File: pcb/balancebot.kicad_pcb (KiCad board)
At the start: 2 copper layers, 31 parts, among them J1 Conn_01x04, J2 Conn_01x02, J3 Conn_01x03, J4 Conn_01x04, J5 Conn_01x04, J6 Conn_01x07, U1 LSM6DS3, U2 DRV8835, U3 ESP32mini, U4 DSN-MINI-360

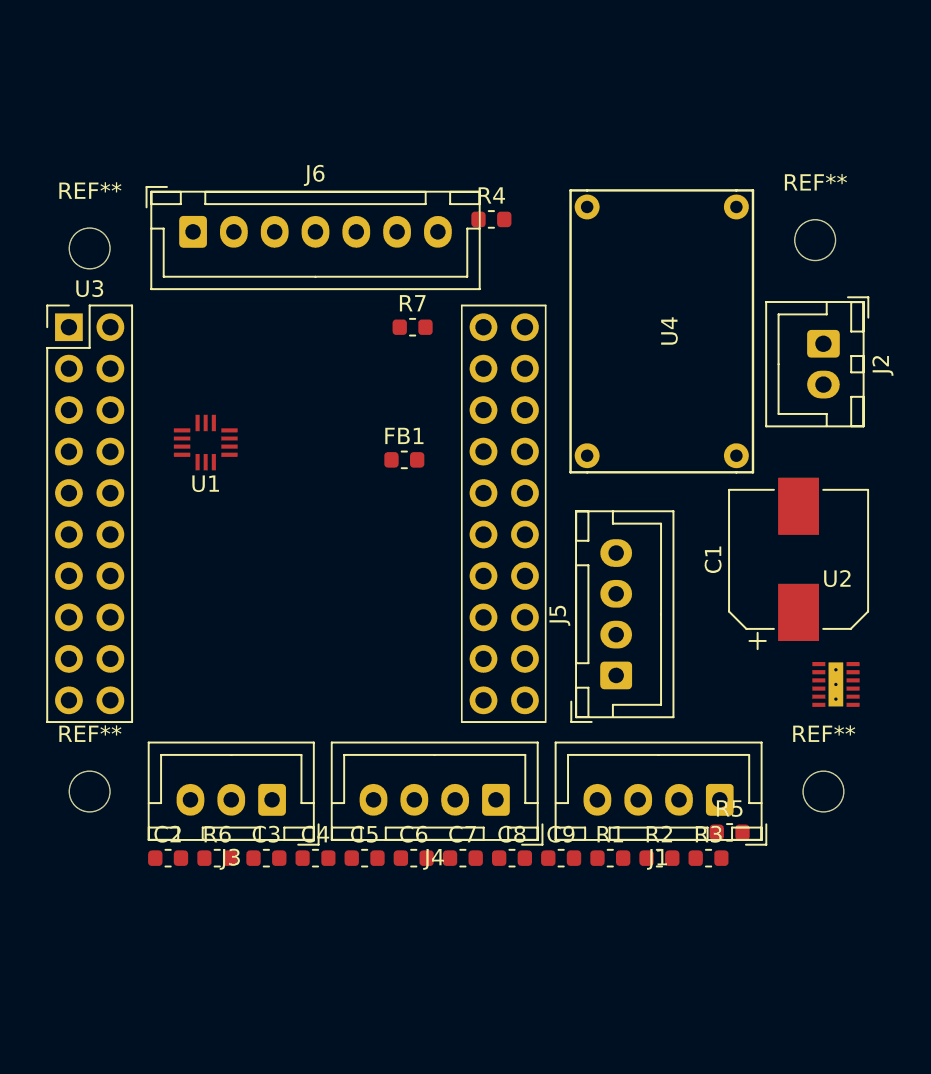
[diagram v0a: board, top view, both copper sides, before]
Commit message: Fix ESP32 footprint.
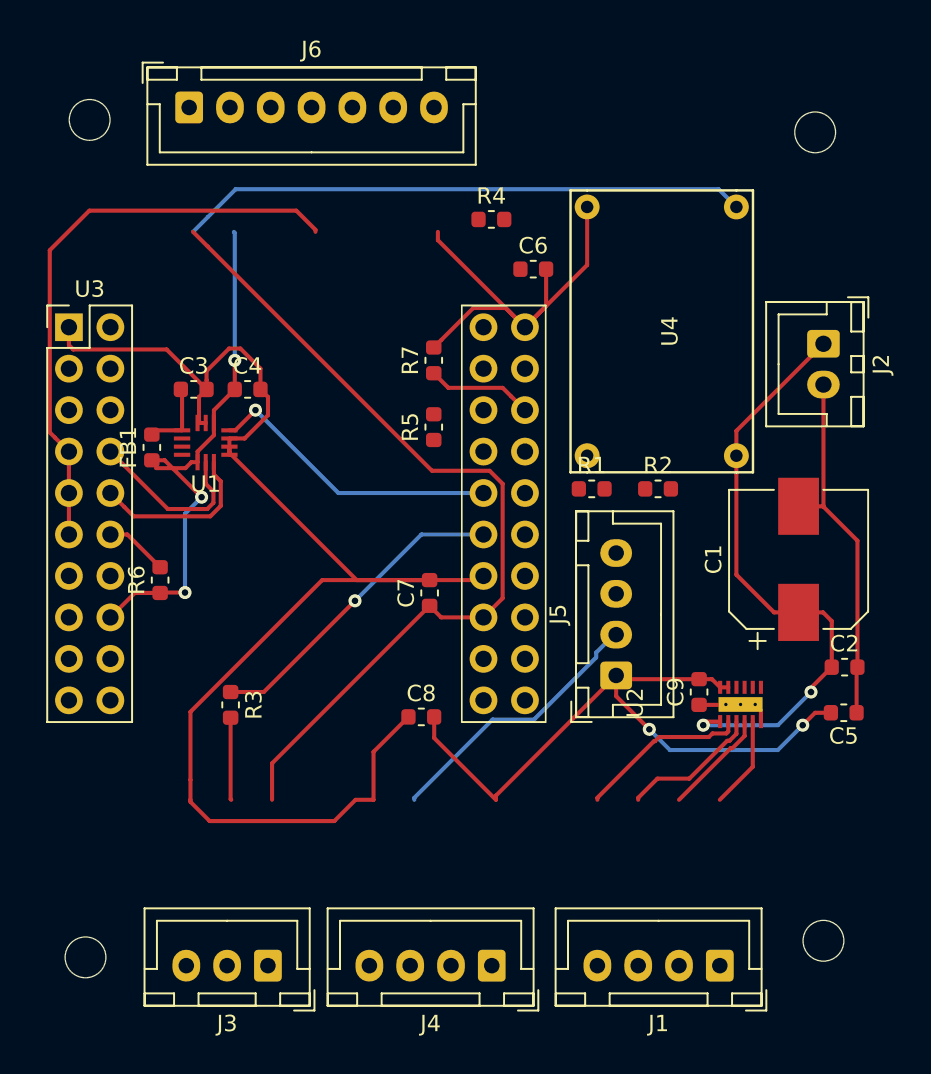
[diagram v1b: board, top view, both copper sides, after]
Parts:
- moved C2 43.1 mm to (164.9, 88.6)
- moved C6 36.8 mm to (145.8, 64.3)
- moved R3 30.8 mm to (127.3, 91.0), turned to 270 degrees
- moved R5 30.7 mm to (139.7, 73.9), turned to 90 degrees
- moved C5 30.7 mm to (164.8, 91.4), turned to 180 degrees
- moved C3 29.1 mm to (125.0, 71.6)
- moved C4 29.0 mm to (128.3, 71.6)
- moved R1 22.7 mm to (149.4, 77.7)
- moved R2 22.6 mm to (153.4, 77.7)
- moved R6 17.4 mm to (122.9, 83.3), turned to 90 degrees
- moved C7 16.4 mm to (139.4, 84.1), turned to 90 degrees
- moved FB1 15.5 mm to (122.4, 75.2), turned to 90 degrees
- moved C9 13.2 mm to (156.0, 90.2), turned to 90 degrees
- moved C8 10.3 mm to (138.9, 91.7)
- moved J3 10.2 mm to (129.5, 106.9)
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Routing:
- net GND: track 0.00 -> 140.3 mm
- net +5V: track 0.00 -> 88.3 mm
- net +3V3: track 0.00 -> 74.5 mm, vias 0 -> 5
- net Net-(J4-Pad3): track 0.00 -> 52.6 mm
- net +BATT: track 0.00 -> 36.8 mm, vias 0 -> 2
- net Net-(R3-Pad1): track 0.00 -> 19.5 mm, vias 0 -> 1
- net IO17: track 0.00 -> 18.2 mm, vias 0 -> 1
- net IO18: track 0.00 -> 10.6 mm
- net IO19: track 0.00 -> 10.5 mm
- net Net-(J1-Pad4): track 0.00 -> 10.4 mm
- net Net-(J1-Pad3): track 0.00 -> 8.52 mm
- net BENBL: track 0.00 -> 6.52 mm
- net Net-(J1-Pad2): track 0.00 -> 6.52 mm
- net Net-(J1-Pad1): track 0.00 -> 5.63 mm
- net Net-(J3-Pad2): track 0.00 -> 5.05 mm
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
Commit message: Complete routing.
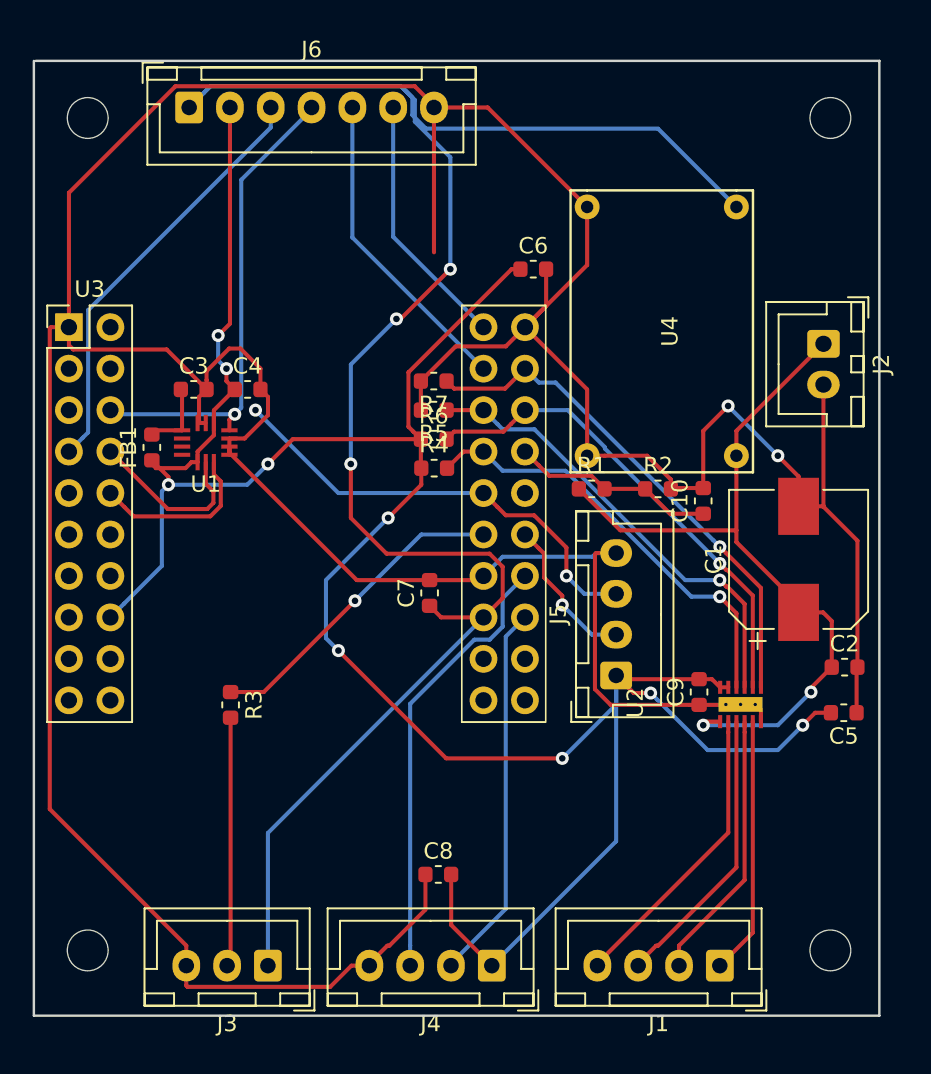
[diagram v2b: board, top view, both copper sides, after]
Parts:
- removed the REF** at (118.4, 106.4)
- removed the REF** at (118.6, 55.1)
- removed the REF** at (163.1, 55.9)
- removed the REF** at (163.6, 105.4)
- added C10: 100n, Capacitor_SMD:C_0603_1608Metric, F.Cu at (156.2, 78.5)
- added REF**: MountingHole_2.5mm, MountingHole:MountingHole_2.5mm, F.Cu at (118.5, 106.0)
- added REF**: MountingHole_2.5mm, MountingHole:MountingHole_2.5mm, F.Cu at (164.0, 106.0)
- added REF**: MountingHole_2.5mm, MountingHole:MountingHole_2.5mm, F.Cu at (164.0, 55.0)
- added REF**: MountingHole_2.5mm, MountingHole:MountingHole_2.5mm, F.Cu at (118.5, 55.0)
- U3: footprint modules:ESP32mini -> BalanceBot:ESP32mini
- U4: footprint dsn-mini-360:DSN-MINI-360 -> BalanceBot:DSN-MINI-360
- moved R6 18.9 mm to (139.7, 74.7), turned to 0 degrees
- moved R4 15.6 mm to (139.7, 76.5)
- moved C8 9.71 mm to (140.0, 101.3)
- moved R7 1.27 mm to (139.7, 71.1), turned to 180 degrees
- moved R5 1.04 mm to (139.7, 72.9), turned to 180 degrees
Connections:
- J4 pad 2: Net-(J4-Pad2) -> IO2
- J4 pad 3: Net-(J4-Pad3) -> IO0
- J5 pad 2: Net-(J4-Pad3) -> IO4
- J5 pad 3: Net-(J4-Pad3) -> IO17
- J6 pad 3: Net-(J6-Pad3) -> IO35
- J6 pad 4: Net-(J4-Pad3) -> IO26
- J6 pad 5: Net-(J6-Pad5) -> RXD
- J6 pad 6: Net-(J6-Pad6) -> TXD
- R1 pad 2: Net-(R1-Pad2) -> IO32
- R2 pad 1: Net-(R1-Pad2) -> IO32
- U1 pad 4: IO17 -> IO26
- U3 pad 11: Net-(J4-Pad3) -> (no net)
- U3 pad 12: BPHASE -> (no net)
- U3 pad 21: (no net) -> TXD
- U3 pad 23: (no net) -> RXD
- U3 pad 24: Net-(J6-Pad3) -> BENBL
- U3 pad 26: BENBL -> BPHASE
- U3 pad 28: Net-(J4-Pad3) -> IO32
- U3 pad 32: Net-(J6-Pad5) -> IO4
- U3 pad 34: Net-(R1-Pad2) -> IO0
- U3 pad 36: Net-(J6-Pad6) -> IO2
- U3 pad 6: Net-(J4-Pad2) -> IO26
- U3 pad 7: Net-(J4-Pad3) -> IO35
- U3 pad 9: Net-(J4-Pad3) -> (no net)
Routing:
- net GND: track 140.3 -> 267.9 mm, vias 0 -> 2
- net +3V3: track 74.5 -> 158.0 mm, vias 5 -> 9
- net Net-(J4-Pad3): track 52.6 -> 0.00 mm
- net IO26: track 0.00 -> 29.6 mm, vias 0 -> 1
- net AENBL: track 0.00 -> 28.3 mm, vias 0 -> 1
- net IO0: track 0.00 -> 27.3 mm
- net APHASE: track 0.00 -> 26.8 mm, vias 0 -> 1
- net IO35: track 0.00 -> 26.2 mm
- net +5V: track 88.3 -> 114.5 mm, vias 0 -> 3
- net BPHASE: track 3.88 -> 29.9 mm, vias 0 -> 1
- net BENBL: track 6.52 -> 31.6 mm, vias 0 -> 1
- net IO2: track 0.00 -> 23.2 mm
- net RXD: track 0.00 -> 19.3 mm
- net TXD: track 0.00 -> 15.8 mm
- net IO32: track 0.00 -> 12.5 mm
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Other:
- board outline added: 51.8 x 58.5 mm

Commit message: Make pretty.
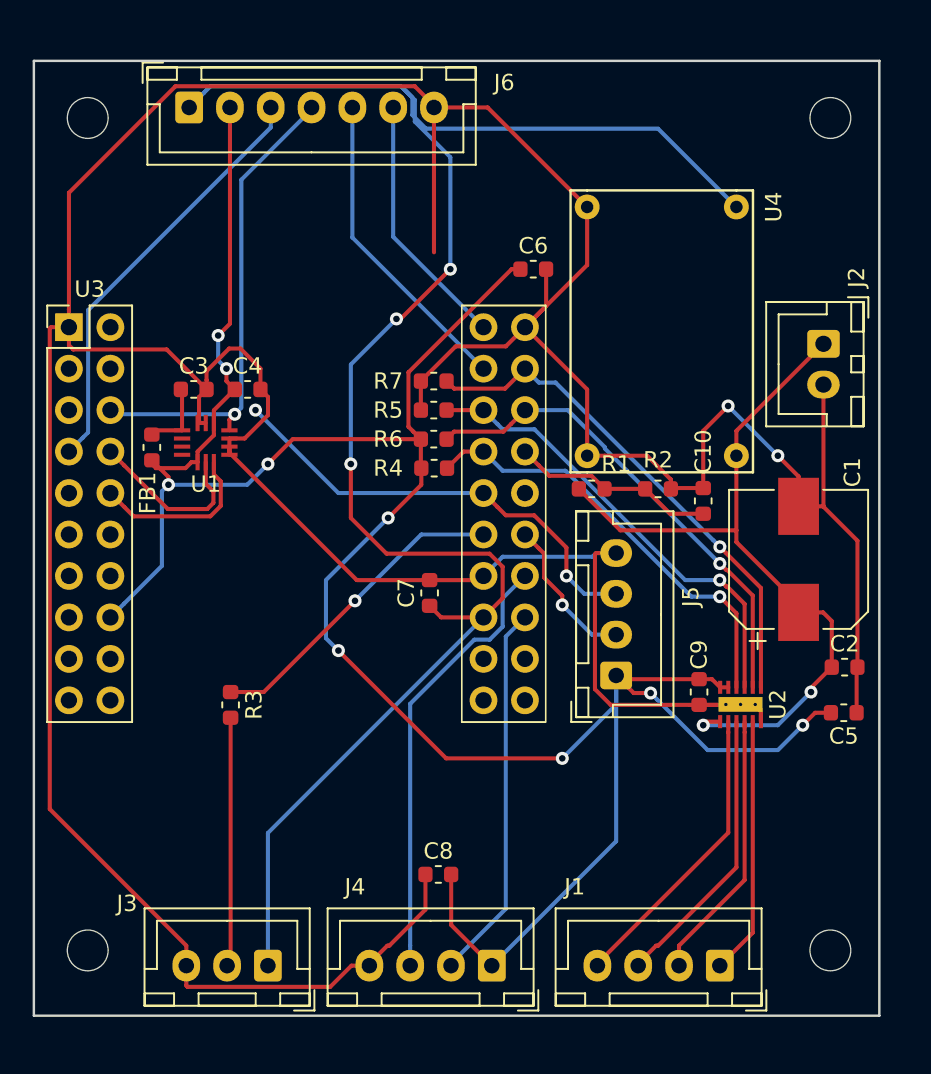
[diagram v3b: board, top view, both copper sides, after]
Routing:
- net GND: track 267.9 -> 273.5 mm
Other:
- outline, holes or cut-outs redrawn
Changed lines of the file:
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@@
     (thickness 1.6)
     (drawings 4)
-    (tracks 355)
+    (tracks 360)
     (zones 0)
     (modules 32)
@@
     (tags resistor)
     (attr smd)
-    (fp_text reference R4 (at 0 -1.43) (layer F.SilkS)
+    (fp_text reference R4 (at -2.8195 0) (layer F.SilkS)
       (effects (font (size 1 1) (thickness 0.15)))
     )
@@
     (tags "Capacitor Electrolytic")
     (attr smd)
-    (fp_text reference C1 (at 0 -5.2 90) (layer F.SilkS)
+    (fp_text reference C1 (at 5.334 3.302 90) (layer F.SilkS)
       (effects (font (size 1 1) (thickness 0.15)))
     )
@@
     (tags capacitor)
     (attr smd)
-    (fp_text reference C9 (at 0 -1.43 90) (layer F.SilkS)
+    (fp_text reference C9 (at 2.286 0 90) (layer F.SilkS)
       (effects (font (size 1 1) (thickness 0.15)))
     )
@@
     (tags inductor)
     (attr smd)
-    (fp_text reference FB1 (at 0 -1.43 90) (layer F.SilkS)
+    (fp_text reference FB1 (at -2.794 -0.254 90) (layer F.SilkS)
       (effects (font (size 1 1) (thickness 0.15)))
     )
@@
     (descr "JST XH series connector, B04B-XH-A (http://www.jst-mfg.com/product/pdf/eng/eXH.pdf), generated with kicad-footprint-generator")
     (tags "connector JST XH side entry")
-    (fp_text reference J1 (at 3.75 -3.55 180) (layer F.SilkS)
+    (fp_text reference J1 (at 8.89 4.826 180) (layer F.SilkS)
       (effects (font (size 1 1) (thickness 0.15)))
     )
@@
     (descr "JST XH series connector, B02B-XH-A (http://www.jst-mfg.com/product/pdf/eng/eXH.pdf), generated with kicad-footprint-generator")
     (tags "connector JST XH side entry")
-    (fp_text reference J2 (at 1.25 -3.55 270) (layer F.SilkS)
+    (fp_text reference J2 (at -4.064 -2.032 270) (layer F.SilkS)
       (effects (font (size 1 1) (thickness 0.15)))
     )
@@
     (descr "JST XH series connector, B03B-XH-A (http://www.jst-mfg.com/product/pdf/eng/eXH.pdf), generated with kicad-footprint-generator")
     (tags "connector JST XH side entry")
-    (fp_text reference J3 (at 2.5 -3.55 180) (layer F.SilkS)
+    (fp_text reference J3 (at 8.636 3.81 180) (layer F.SilkS)
       (effects (font (size 1 1) (thickness 0.15)))
     )
@@
     (descr "JST XH series connector, B04B-XH-A (http://www.jst-mfg.com/product/pdf/eng/eXH.pdf), generated with kicad-footprint-generator")
     (tags "connector JST XH side entry")
-    (fp_text reference J4 (at 3.75 -3.55 180) (layer F.SilkS)
+    (fp_text reference J4 (at 8.382 4.826 180) (layer F.SilkS)
       (effects (font (size 1 1) (thickness 0.15)))
     )
@@
     (descr "JST XH series connector, B04B-XH-A (http://www.jst-mfg.com/product/pdf/eng/eXH.pdf), generated with kicad-footprint-generator")
     (tags "connector JST XH side entry")
-    (fp_text reference J5 (at 3.75 -3.55 90) (layer F.SilkS)
+    (fp_text reference J5 (at 4.826 4.572 90) (layer F.SilkS)
       (effects (font (size 1 1) (thickness 0.15)))
     )
@@
     (descr "JST XH series connector, B07B-XH-A (http://www.jst-mfg.com/product/pdf/eng/eXH.pdf), generated with kicad-footprint-generator")
     (tags "connector JST XH side entry")
-    (fp_text reference J6 (at 7.5 -3.55) (layer F.SilkS)
+    (fp_text reference J6 (at 19.304 -1.524) (layer F.SilkS)
       (effects (font (size 1 1) (thickness 0.15)))
     )
@@
     (tags resistor)
     (attr smd)
-    (fp_text reference R1 (at 0 -1.43) (layer F.SilkS)
+    (fp_text reference R1 (at 1.4985 -1.524) (layer F.SilkS)
       (effects (font (size 1 1) (thickness 0.15)))
     )
@@
     (tags resistor)
     (attr smd)
-    (fp_text reference R2 (at 0 -1.43) (layer F.SilkS)
+    (fp_text reference R2 (at 0 -1.778) (layer F.SilkS)
       (effects (font (size 1 1) (thickness 0.15)))
     )
@@
     (tags resistor)
     (attr smd)
-    (fp_text reference R5 (at 0 -1.43 180) (layer F.SilkS)
+    (fp_text reference R5 (at 2.794 0 180) (layer F.SilkS)
       (effects (font (size 1 1) (thickness 0.15)))
     )
@@
     (tags resistor)
     (attr smd)
-    (fp_text reference R6 (at 0 -1.43) (layer F.SilkS)
+    (fp_text reference R6 (at -2.794 0) (layer F.SilkS)
       (effects (font (size 1 1) (thickness 0.15)))
     )
@@
     (tags resistor)
     (attr smd)
-    (fp_text reference R7 (at 0 -1.43 180) (layer F.SilkS)
+    (fp_text reference R7 (at 2.794 0 180) (layer F.SilkS)
       (effects (font (size 1 1) (thickness 0.15)))
     )
@@
   (module BalanceBot:WSON-12 (layer F.Cu)
     (at 161.246 90.932 90)
-    (fp_text reference U2 (at 0.1 -9.2 90) (layer F.SilkS)
+    (fp_text reference U2 (at 0 -0.464 90) (layer F.SilkS)
       (effects (font (size 1 1) (thickness 0.15)))
     )
@@
     (tags capacitor)
     (attr smd)
-    (fp_text reference C10 (at 0 -1.43 90) (layer F.SilkS)
+    (fp_text reference C10 (at 3.0225 0 90) (layer F.SilkS)
       (effects (font (size 1 1) (thickness 0.15)))
     )
@@
   (module BalanceBot:DSN-MINI-360 (layer F.Cu)
     (at 153.67 68.072 90)
-    (fp_text reference U4 (at 0 0.5 90) (layer F.SilkS)
+    (fp_text reference U4 (at 7.62 6.858 90) (layer F.SilkS)
       (effects (font (size 1 1) (thickness 0.15)))
     )
@@
     (pad 1 np_thru_hole circle (at 0 0) (size 2.5 2.5) (drill 2.5) (layers *.Cu *.Mask))
   )
-  (gr_line (start 167 51.5) (end 115.316 51.5) (layer Edge.Cuts) (width 0.15))
+  (gr_line (start 167 51.5) (end 115.2 51.5) (layer Edge.Cuts) (width 0.15))
   (gr_line (start 167 110) (end 167 51.5) (layer Edge.Cuts) (width 0.15))
   (gr_line (start 115.2 110) (end 167 110) (layer Edge.Cuts) (width 0.15))
-  (gr_line (start 115.2 51.5) (end 115.2 109.982) (layer Edge.Cuts) (width 0.15))
+  (gr_line (start 115.2 51.5) (end 115.2 110) (layer Edge.Cuts) (width 0.15))
   (segment (start 158.242 74.168) (end 158.242 75.692) (width 0.25) (layer F.Cu) (net 1) (status 20))
   (segment (start 163.576 68.834) (end 158.242 74.168) (width 0.25) (layer F.Cu) (net 1) (status 10))
@@
   (segment (start 116.172999 97.341999) (end 124.54 105.709) (width 0.25) (layer F.Cu) (net 2))
   (segment (start 117.348 67.818) (end 116.248 67.818) (width 0.25) (layer F.Cu) (net 2))
+  (segment (start 158.4705 90.9575) (end 158.496 90.932) (width 0.25) (layer F.Cu) (net 2))
+  (segment (start 155.956 90.9575) (end 158.4705 90.9575) (width 0.25) (layer F.Cu) (net 2))
+  (segment (start 159.746 91.332) (end 159.746 91.982) (width 0.25) (layer F.Cu) (net 2))
+  (segment (start 159.346 90.932) (end 159.746 91.332) (width 0.25) (layer F.Cu) (net 2))
+  (segment (start 157.596 90.932) (end 159.346 90.932) (width 0.25) (layer F.Cu) (net 2))
   (segment (start 124.28 71.702) (end 124.206 71.628) (width 0.25) (layer F.Cu) (net 3) (status 30))
   (segment (start 124.28 74.136) (end 124.28 71.702) (width 0.25) (layer F.Cu) (net 3) (status 30))

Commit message: Update ESP32 footprint; make motor traces wider.
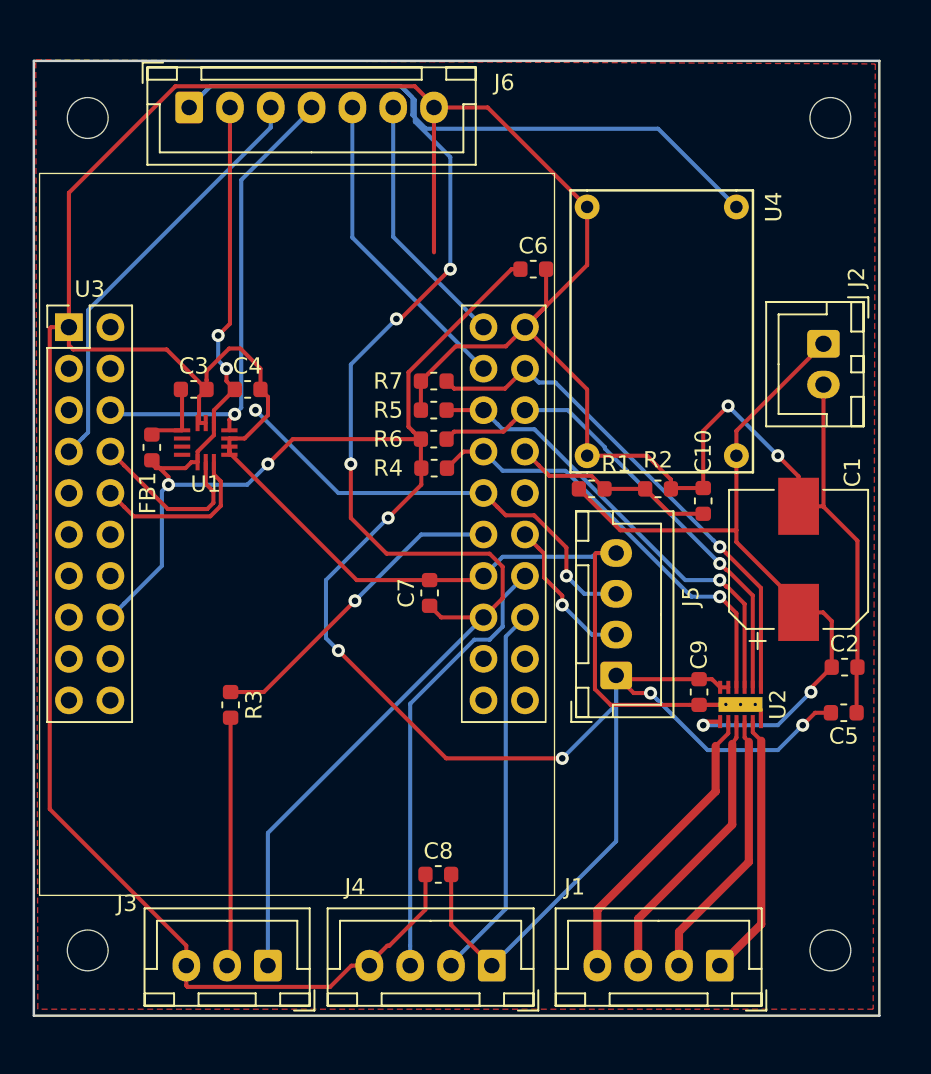
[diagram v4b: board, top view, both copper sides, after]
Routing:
- added copper zone on F.Cu, net GND
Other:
- net class Thicc added: clearance 0.2, trace_width 1, via_dia 0.8, via_drill 0.4

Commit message: Finalize PCB.
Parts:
- added REF**: OSHW-Logo2_7.3x6mm_SilkScreen, Symbol:OSHW-Logo2_7.3x6mm_SilkScreen, F.Cu at (153.0, 55.2)
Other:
- board text added: "BalanceBot"
- board text added: "https://github.com/bullestock/balancebot"
